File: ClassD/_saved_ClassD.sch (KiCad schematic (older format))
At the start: 52 parts, among them P1 RedRCA, P2 WhiteRCA, P3 CONN_01X02, P4 CONN_01X02, P5 CONN_01X02, SW1 SW_PUSH, SW2 SW_PUSH, U1 TDA7491LP, U2 MCP1700T

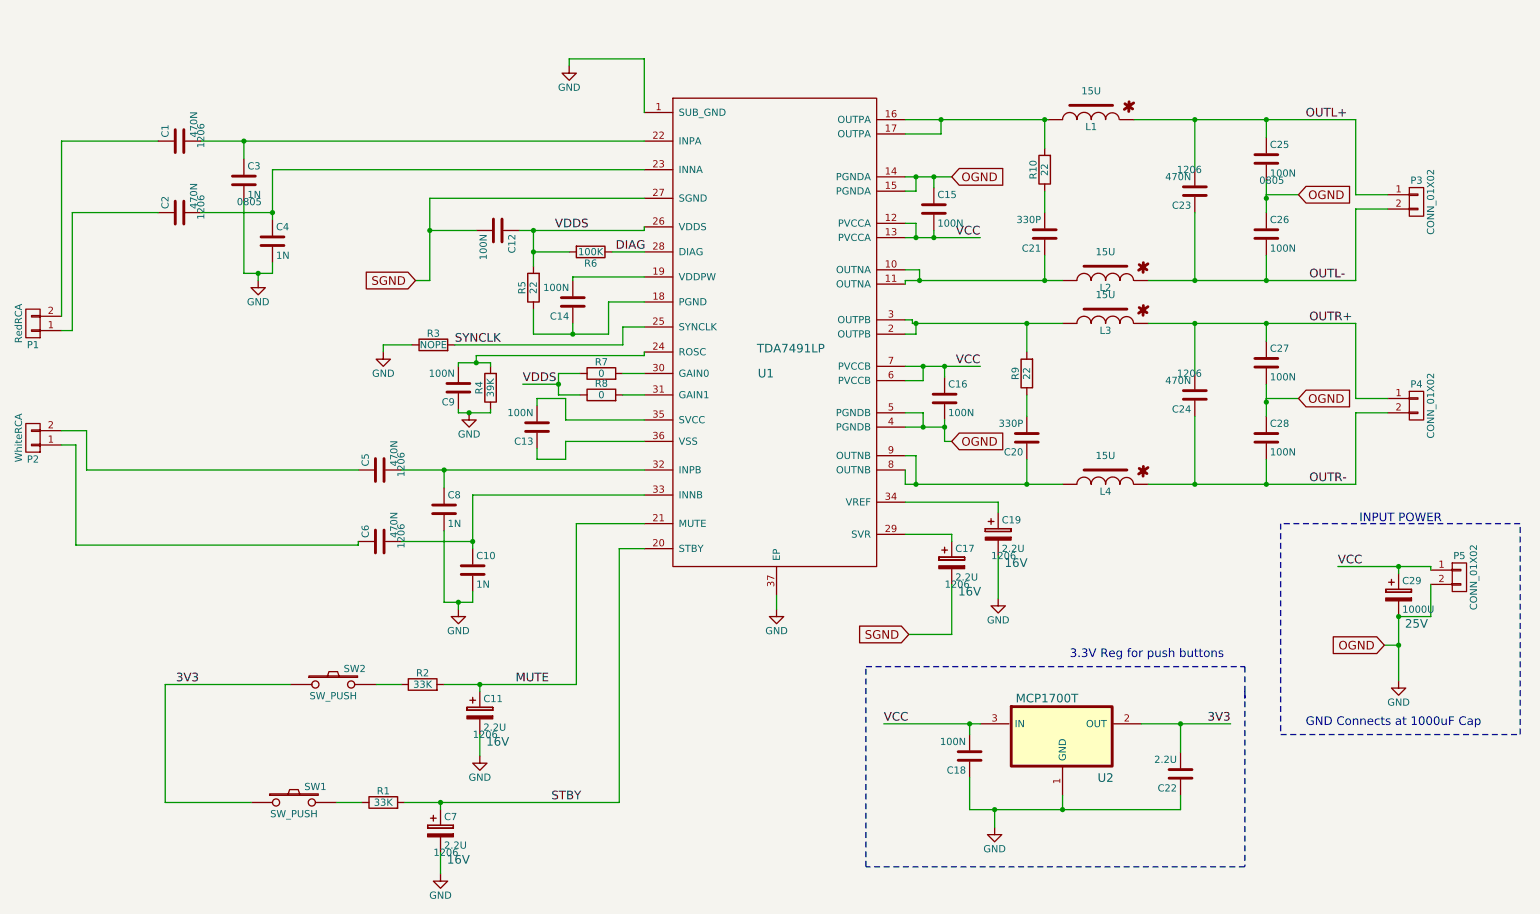
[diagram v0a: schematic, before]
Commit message: Created and associated all footprints
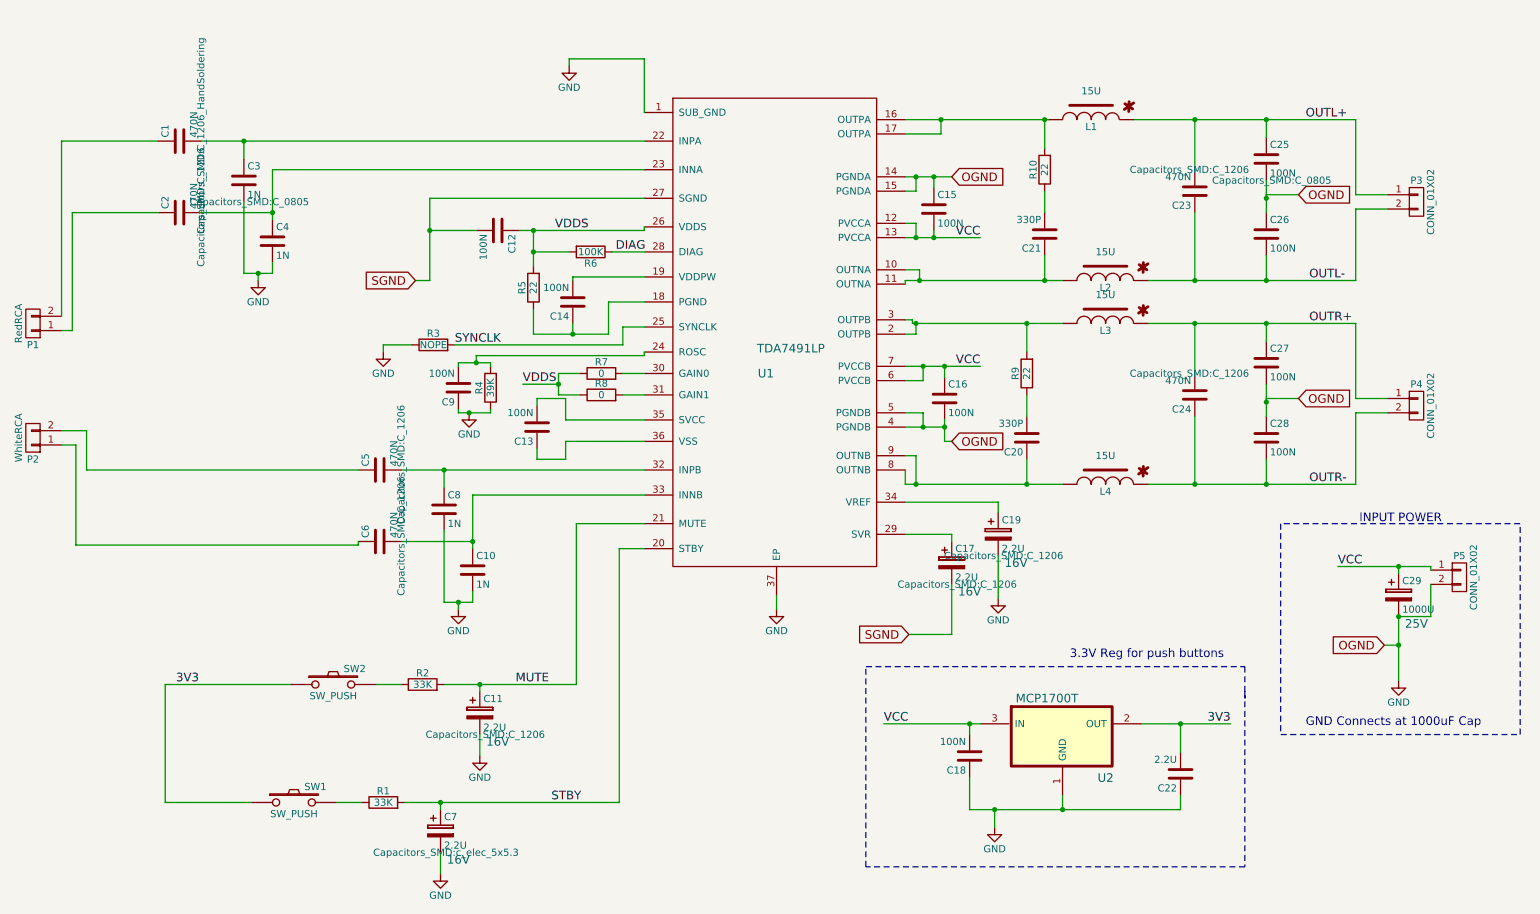
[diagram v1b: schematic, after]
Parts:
- C1: footprint 1206 -> Capacitors_SMD:C_1206_HandSoldering
- C10, C12, C13, C14, C15, C16, C18, C20, C21, C26, C27, C28, C4, C8, C9: footprint (none) -> Capacitors_SMD:C_0805
- C11, C17, C19, C2, C23, C24, C5, C6: footprint 1206 -> Capacitors_SMD:C_1206
- C22: footprint (none) -> Capacitors_SMD:C_1206
- C25, C3: footprint 0805 -> Capacitors_SMD:C_0805
- C29: footprint (none) -> ClassD:c_elec_13.6x13.6
- C7: footprint 1206 -> Capacitors_SMD:c_elec_5x5.3
- L1, L2, L3, L4: footprint (none) -> ClassD:NRS6045T150MMGK
- P1, P2: footprint (none) -> ClassD:RCJ1x
- P3, P4, P5: footprint (none) -> Pin_Headers:Pin_Header_Straight_1x02
- R1, R10, R2, R3, R4, R5, R6, R7, R8, R9: footprint (none) -> Resistors_SMD:R_0805
- SW1, SW2: footprint (none) -> ClassD:FSM2JSMAA-ND
- U2: footprint (none) -> TO_SOT_Packages_SMD:SOT-23
